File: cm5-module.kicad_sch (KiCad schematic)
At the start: 0 parts

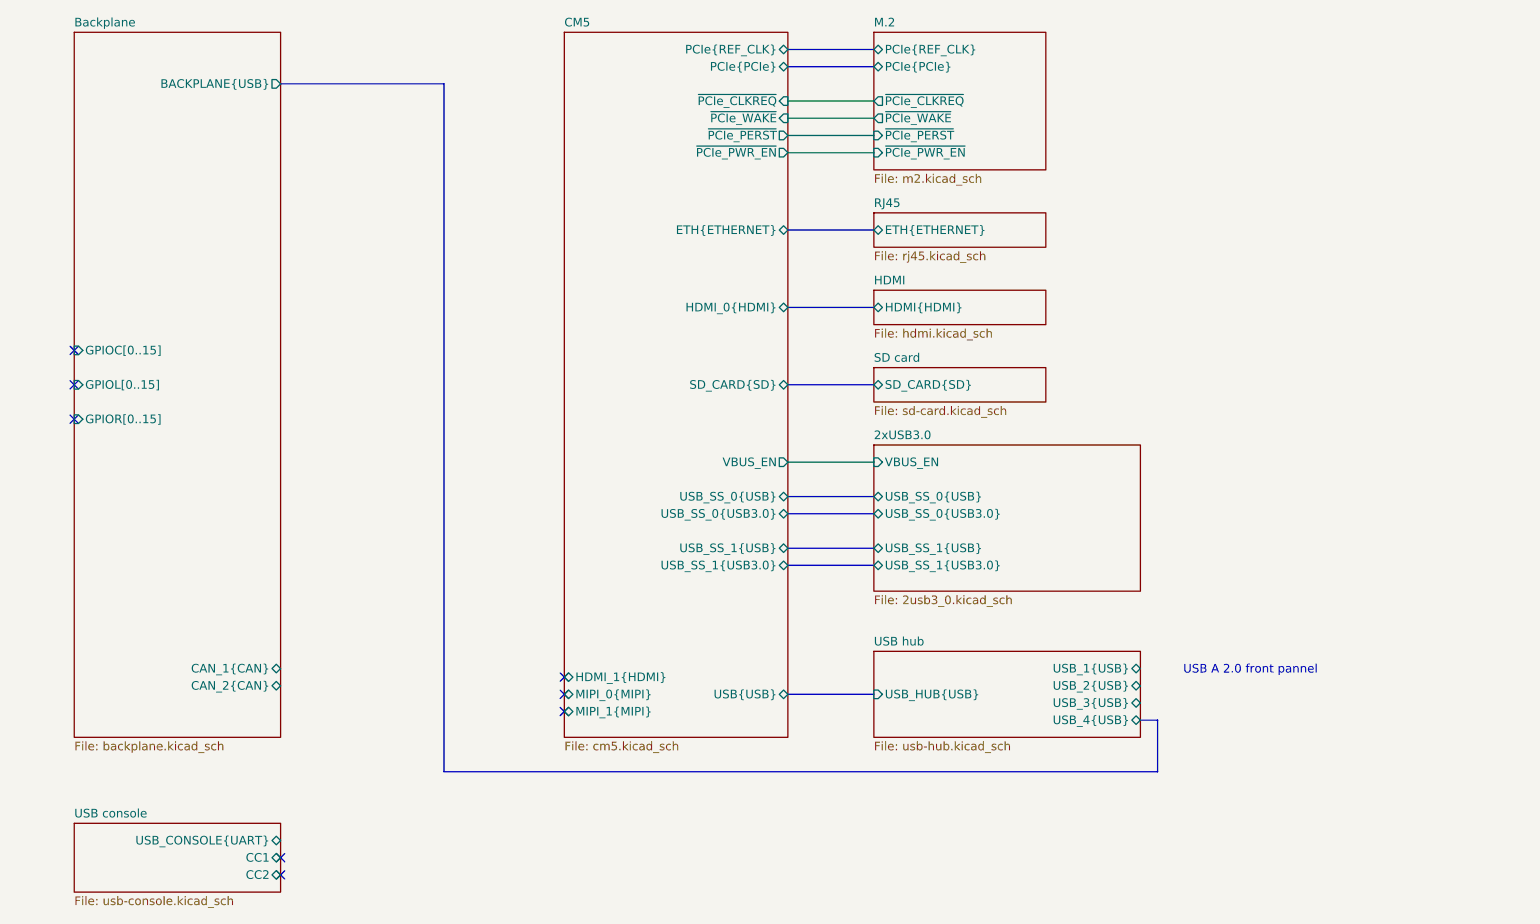
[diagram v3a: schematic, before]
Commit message: [#1] Add debug UART connector
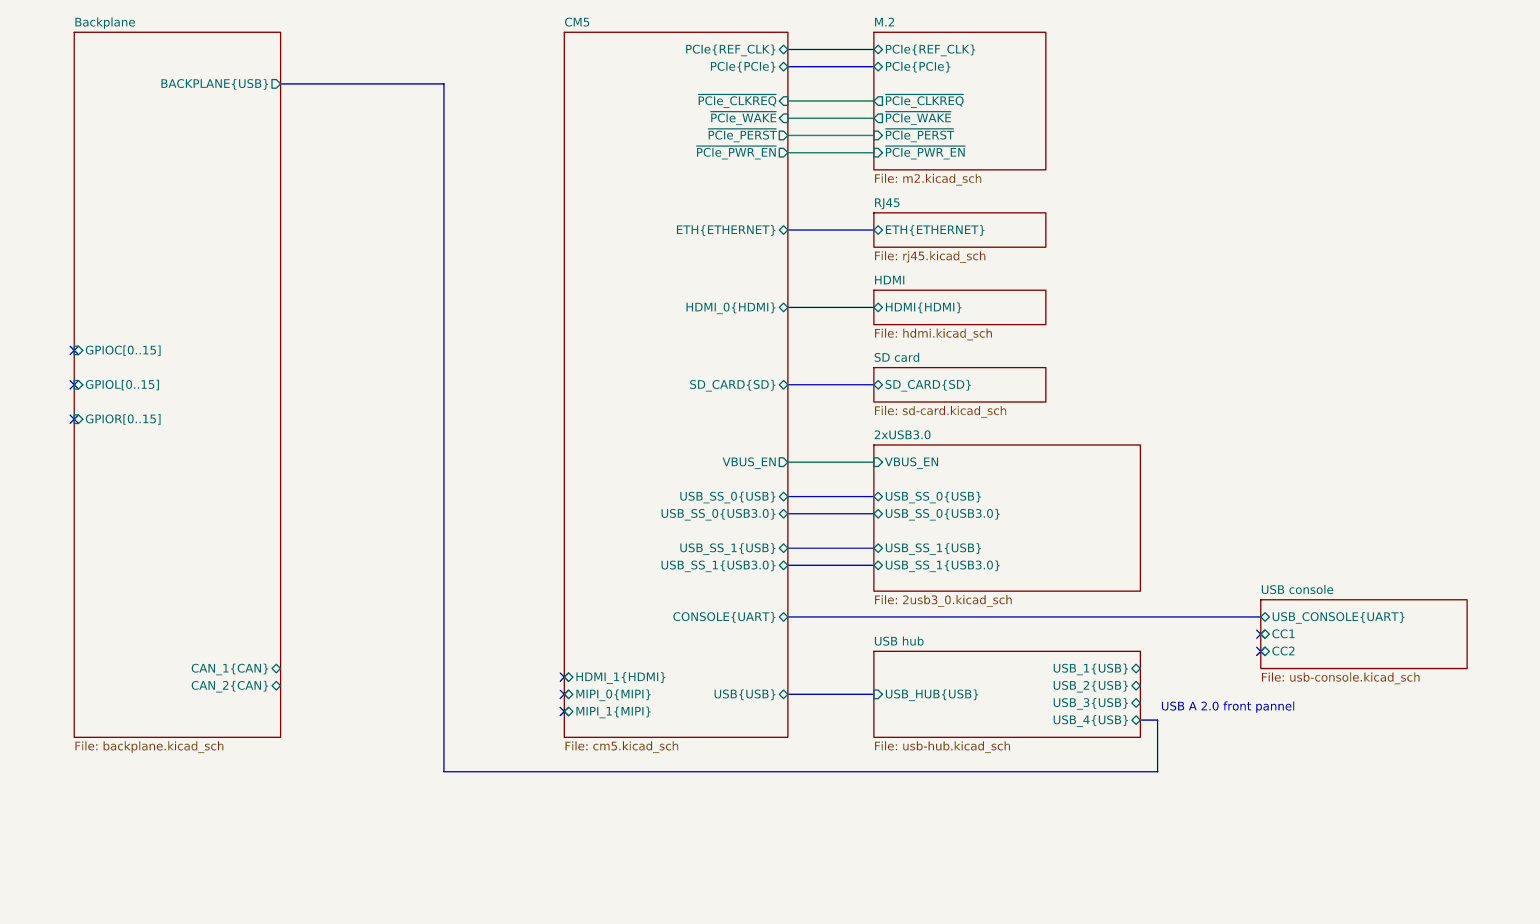
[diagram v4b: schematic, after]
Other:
- sheet CM5 ports: added CONSOLE{UART}; removed none
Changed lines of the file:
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@@
 	(text "USB A 2.0 front pannel"
 		(exclude_from_sim no)
-		(at 220.726 132.334 0)
+		(at 217.424 137.922 0)
 		(effects
 			(font
@@
 	)
 	(no_connect
-		(at 77.47 162.56)
+		(at 222.25 129.54)
 	)
 	(no_connect
@@
 	)
 	(no_connect
-		(at 77.47 160.02)
+		(at 222.25 127)
 	)
 	(no_connect
@@
 		)
 	)
+	(bus
+		(pts
+			(xy 152.4 124.46) (xy 222.25 124.46)
+		)
+		(stroke
+			(width 0)
+			(type default)
+		)
+	)
 	(wire
 		(pts
@@
 	)
 	(sheet
-		(at 46.99 154.94)
+		(at 222.25 121.92)
 		(size 30.48 10.16)
 		(exclude_from_sim no)
@@
 		)
 		(property "Sheetname" "USB console"
-			(at 46.99 154.2284 0)
+			(at 222.25 121.2084 0)
 			(effects
 				(font
@@
 		)
 		(property "Sheetfile" "usb-console.kicad_sch"
-			(at 46.99 165.6846 0)
+			(at 222.25 132.6646 0)
 			(effects
 				(font
@@
 		)
 		(pin "USB_CONSOLE{UART}" bidirectional
-			(at 77.47 157.48 0)
-			(effects
-				(font
-					(size 1.27 1.27)
-				)
-				(justify right)
+			(at 222.25 124.46 180)
+			(effects
+				(font
+					(size 1.27 1.27)
+				)
+				(justify left)
 			)
 		)
 		(pin "CC1" bidirectional
-			(at 77.47 160.02 0)
-			(effects
-				(font
-					(size 1.27 1.27)
-				)
-				(justify right)
+			(at 222.25 127 180)
+			(effects
+				(font
+					(size 1.27 1.27)
+				)
+				(justify left)
 			)
 		)
 		(pin "CC2" bidirectional
-			(at 77.47 162.56 0)
-			(effects
-				(font
-					(size 1.27 1.27)
-				)
-				(justify right)
+			(at 222.25 129.54 180)
+			(effects
+				(font
+					(size 1.27 1.27)
+				)
+				(justify left)
 			)
 		)
@@
 			(effects
 				(font
+					(size 1.27 1.27)
+				)
+				(justify right)
+			)
+		)
+		(pin "CONSOLE{UART}" bidirectional
+			(at 152.4 124.46 0)
+			(effects
+				(font

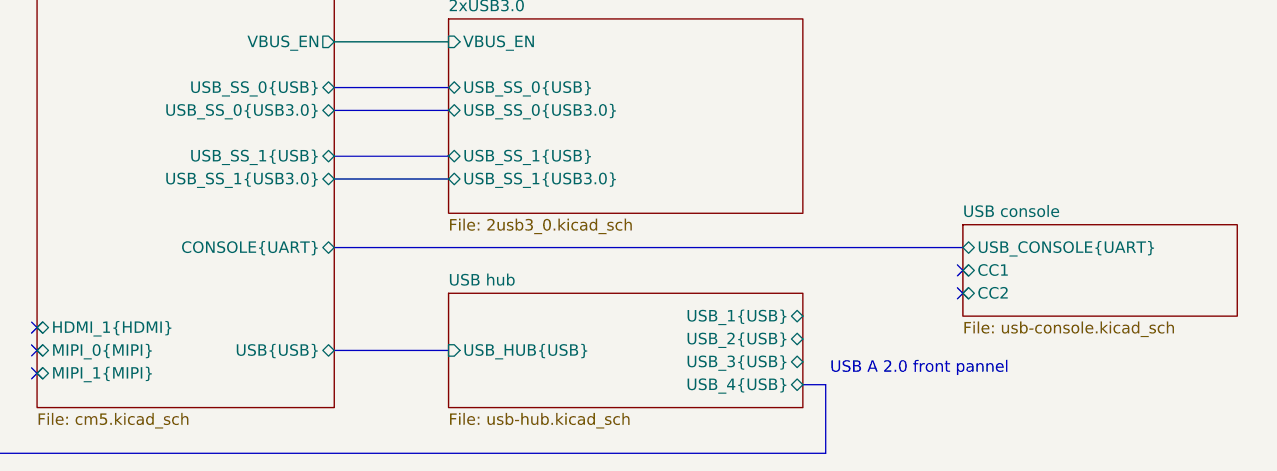
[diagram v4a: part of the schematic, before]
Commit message: [#1] Add level shifter for UART debug, update footprints from library
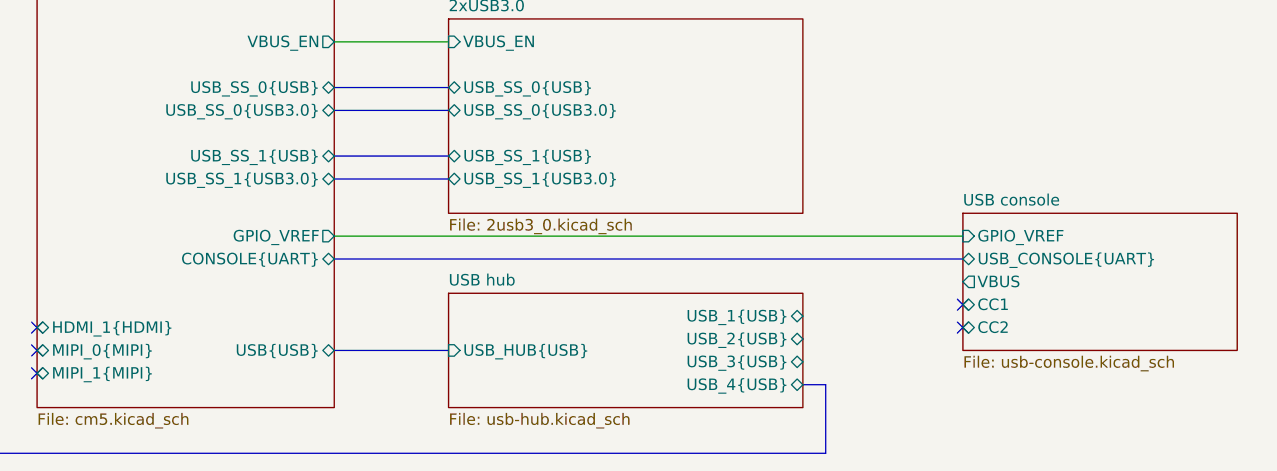
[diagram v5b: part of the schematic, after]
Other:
- sheet CM5 ports: added GPIO_VREF; removed none
- sheet USB console ports: added GPIO_VREF, VBUS; removed none
- note removed: "USB A 2.0 front pannel"
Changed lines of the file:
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@@
 		(members "+" "-")
-	)
-	(text "USB A 2.0 front pannel"
-		(exclude_from_sim no)
-		(at 217.424 137.922 0)
-		(effects
-			(font
-				(size 1.27 1.27)
-			)
-		)
 	)
 	(no_connect
@@
 	)
 	(no_connect
-		(at 222.25 129.54)
+		(at 222.25 133.35)
 	)
 	(no_connect
@@
 	)
 	(no_connect
-		(at 222.25 127)
+		(at 222.25 130.81)
 	)
 	(no_connect
@@
 	(bus
 		(pts
-			(xy 152.4 124.46) (xy 222.25 124.46)
+			(xy 152.4 125.73) (xy 222.25 125.73)
 		)
 		(stroke
@@
 		)
 	)
+	(wire
+		(pts
+			(xy 152.4 123.19) (xy 222.25 123.19)
+		)
+		(stroke
+			(width 0)
+			(type default)
+		)
+	)
 	(bus
 		(pts
@@
 	)
 	(sheet
-		(at 222.25 121.92)
-		(size 30.48 10.16)
+		(at 222.25 120.65)
+		(size 30.48 15.24)
 		(exclude_from_sim no)
 		(in_bom yes)
@@
 		)
 		(property "Sheetname" "USB console"
-			(at 222.25 121.2084 0)
+			(at 222.25 119.9384 0)
 			(effects
 				(font
@@
 		)
 		(property "Sheetfile" "usb-console.kicad_sch"
-			(at 222.25 132.6646 0)
+			(at 222.25 136.4746 0)
 			(effects
 				(font
@@
 		)
 		(pin "USB_CONSOLE{UART}" bidirectional
-			(at 222.25 124.46 180)
+			(at 222.25 125.73 180)
 			(effects
 				(font
@@
 		)
 		(pin "CC1" bidirectional
-			(at 222.25 127 180)
+			(at 222.25 130.81 180)
 			(effects
 				(font
@@
 		)
 		(pin "CC2" bidirectional
-			(at 222.25 129.54 180)
+			(at 222.25 133.35 180)
+			(effects
+				(font
+					(size 1.27 1.27)
+				)
+				(justify left)
+			)
+		)
+		(pin "VBUS" output
+			(at 222.25 128.27 180)
+			(effects
+				(font
+					(size 1.27 1.27)
+				)
+				(justify left)
+			)
+		)
+		(pin "GPIO_VREF" input
+			(at 222.25 123.19 180)
 			(effects
 				(font
@@
 		)
 		(pin "CONSOLE{UART}" bidirectional
-			(at 152.4 124.46 0)
-			(effects
-				(font
+			(at 152.4 125.73 0)
+			(effects
+				(font
+					(size 1.27 1.27)
+				)
+				(justify right)
+			)
+		)
+		(pin "GPIO_VREF" output
+			(at 152.4 123.19 0)
+			(effects
+				(font

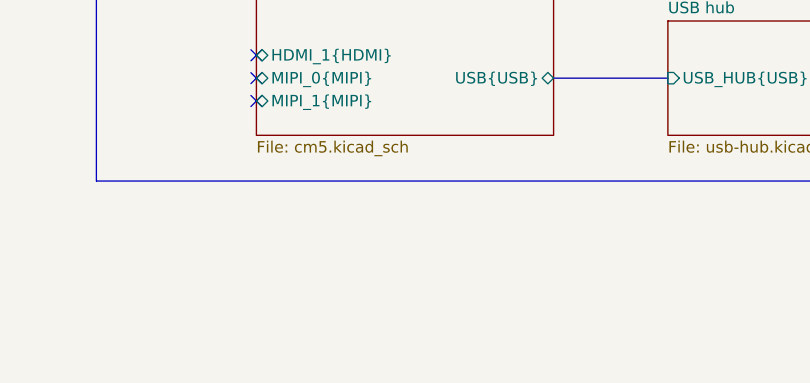
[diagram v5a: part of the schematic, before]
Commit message: [#1] Add power section
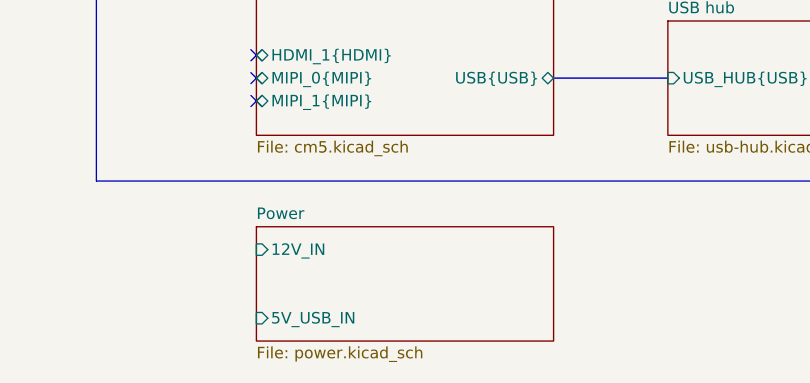
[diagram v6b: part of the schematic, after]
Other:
- added sheet Power (power.kicad_sch)
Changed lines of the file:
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@@
+	)
+	(sheet
+		(at 119.38 152.4)
+		(size 33.02 12.7)
+		(exclude_from_sim no)
+		(in_bom yes)
+		(on_board yes)
+		(dnp no)
+		(fields_autoplaced yes)
+		(stroke
+			(width 0.1524)
+			(type solid)
+		)
+		(fill
+			(color 255 255 194 1.0000)
+		)
+		(property "Sheetname" "Power"
+			(at 119.38 151.6884 0)
+			(effects
+				(font
+					(size 1.27 1.27)
+				)
+				(justify left bottom)
+			)
+		)
+		(property "Sheetfile" "power.kicad_sch"
+			(at 119.38 165.6846 0)
+			(effects
+				(font
+					(size 1.27 1.27)
+				)
+				(justify left top)
+			)
+		)
+		(pin "12V_IN" input
+			(at 119.38 154.94 180)
+			(effects
+				(font
+					(size 1.27 1.27)
+				)
+				(justify left)
+			)
+		)
+		(pin "5V_USB_IN" input
+			(at 119.38 162.56 180)
+			(effects
+				(font
+					(size 1.27 1.27)
+				)
+				(justify left)
+			)
+		)
+		(instances
+			(project "cm5-module"
+				(path "/090a8e41-87a8-4fb1-998b-60a2c0dc4cee"
+					(page "11")
+				)
+			)
+		)
 	)
 	(sheet

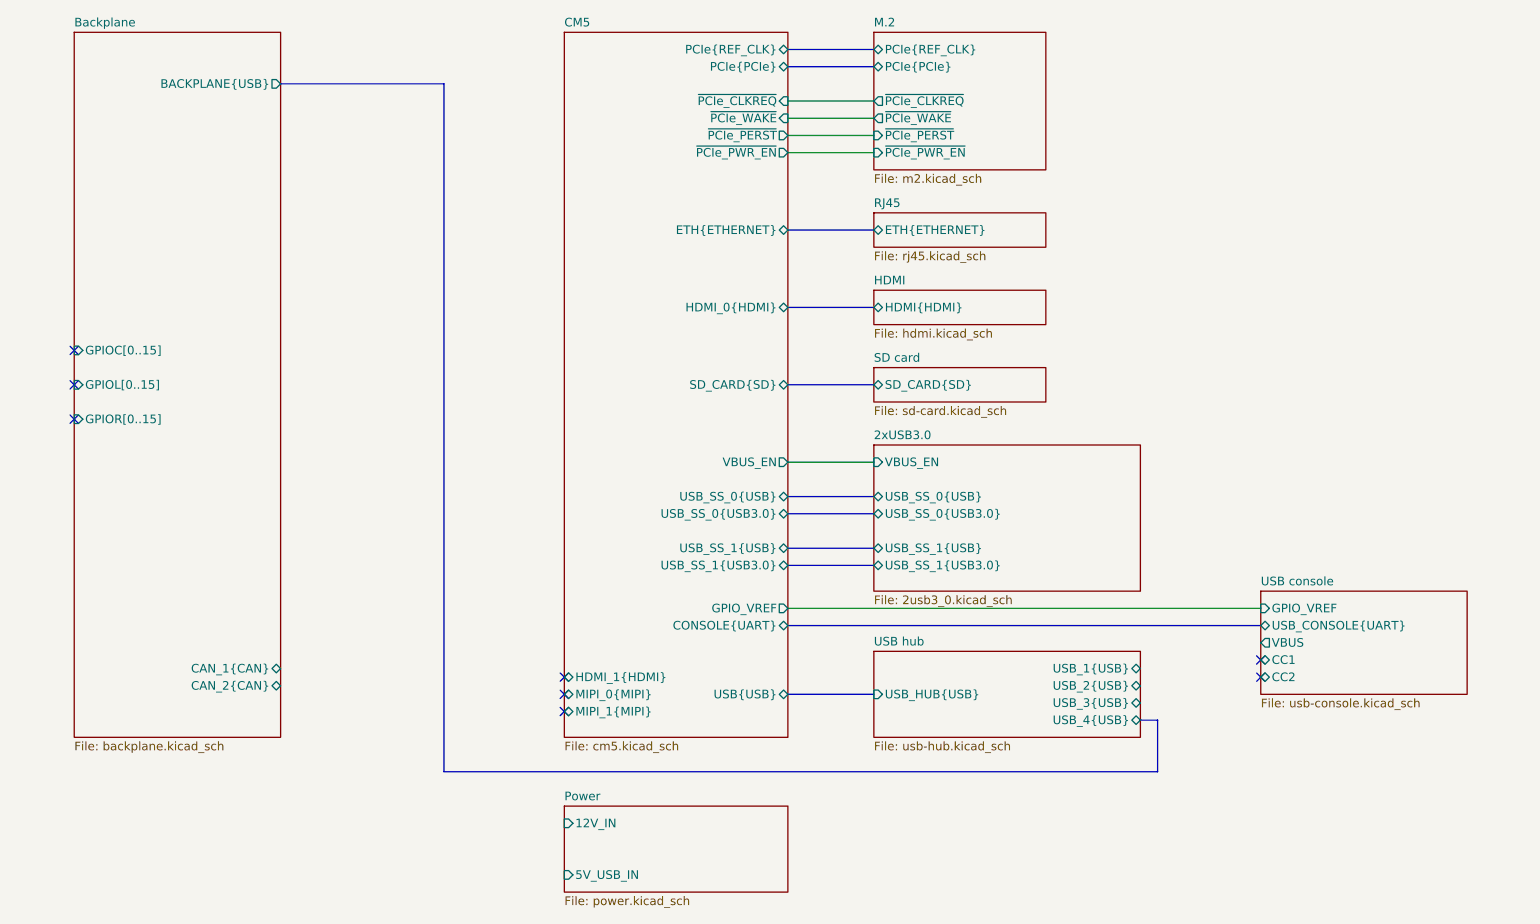
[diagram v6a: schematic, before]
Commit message: [#1] WIP: Refactor schematic
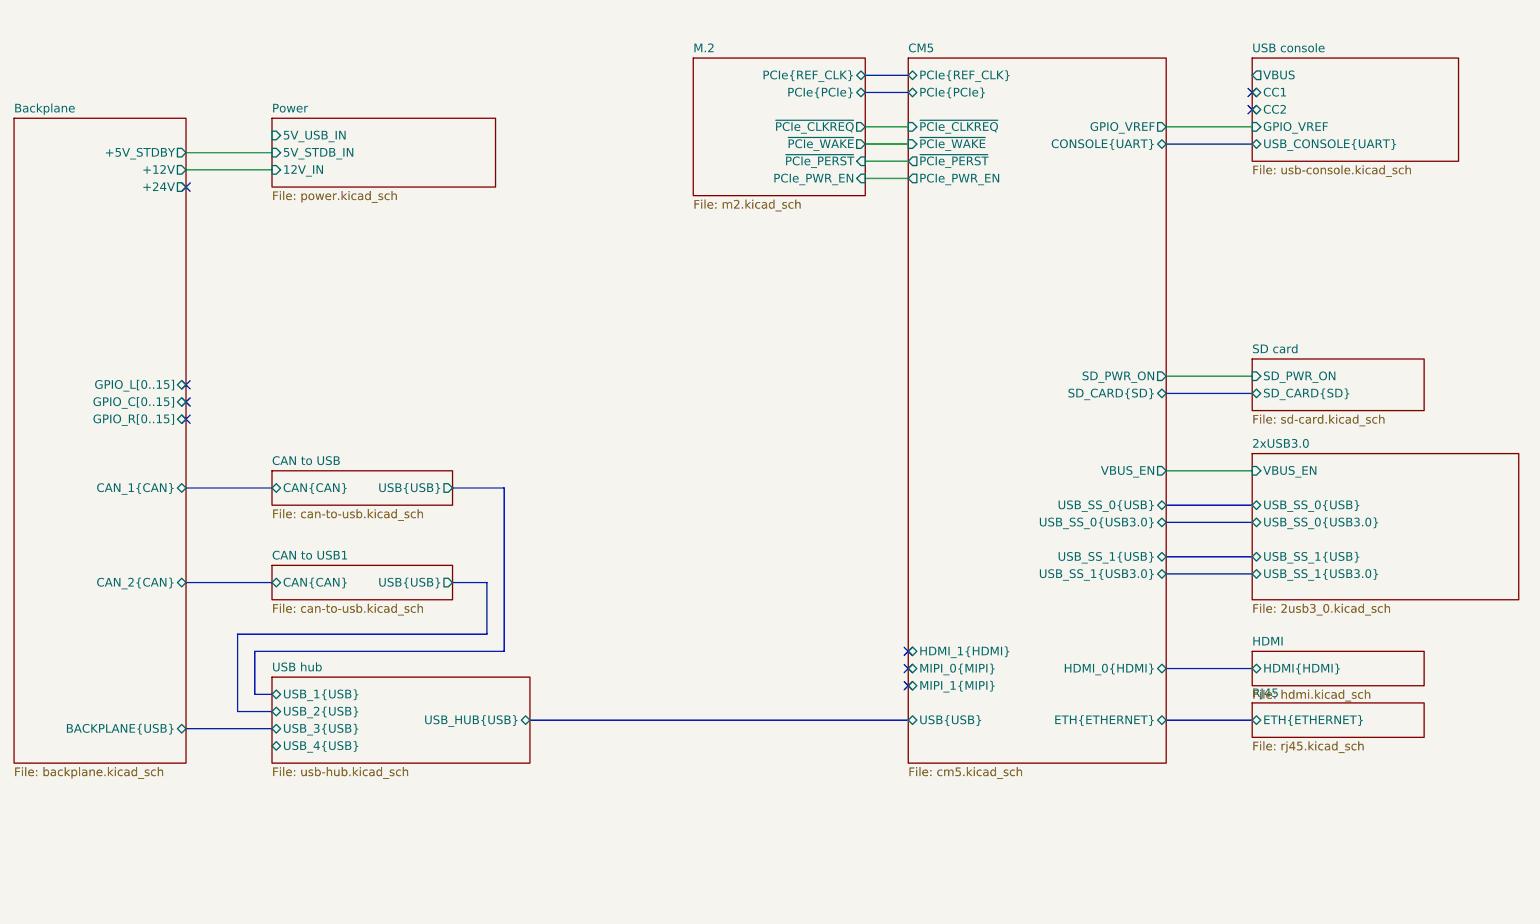
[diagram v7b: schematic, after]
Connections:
- no-connect marks 8 -> 9
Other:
- added sheet CAN to USB (can-to-usb.kicad_sch)
- added sheet CAN to USB1 (can-to-usb.kicad_sch)
- sheet Backplane ports: added +12V, +24V, +5V_STDBY, GPIO_C[0..15], GPIO_L[0..15], GPIO_R[0..15]; removed GPIOC[0..15], GPIOL[0..15], GPIOR[0..15]
- sheet CM5 ports: added PCIe_PWR_EN, SD_PWR_ON; removed ~{PCIe_PWR_EN}
- sheet M.2 ports: added PCIe_PWR_EN; removed ~{PCIe_PWR_EN}
- sheet Power ports: added 5V_STDB_IN; removed none
- sheet SD card ports: added SD_PWR_ON; removed none
